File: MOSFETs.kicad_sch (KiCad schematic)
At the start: 40 parts, among them J4 Motor, J6 Sol_1, J7 Sol_2, J8 Sol_3, J9 Sol_4, Q1 IRF520N, Q2 IRF520N, Q3 IRF520N, Q4 IRF520N, Q5 IRF520N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

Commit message: working: continue at Work.
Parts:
- J4, J6, J7, J8, J9: footprint TerminalBlock_Phoenix:TerminalBlock_Phoenix_PT-1,5-2-5.0-H_1x02_P5.00mm_Horizontal -> TerminalBlock_RND:TerminalBlock_RND_205-00276_1x02_P5.00mm_Vertical
- R10, R11, R12, R13, R14, R15, R16, R17, R22, R23, R24, R25, R26, R8, R9: footprint Resistor_THT:R_Axial_DIN0309_L9.0mm_D3.2mm_P12.70mm_Horizontal -> Resistor_SMD:R_1206_3216Metric_Pad1.30x1.75mm_HandSolder
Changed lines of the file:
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@@
 			)
 		)
-		(property "Footprint" "TerminalBlock_Phoenix:TerminalBlock_Phoenix_PT-1,5-2-5.0-H_1x02_P5.00mm_Horizontal"
+		(property "Footprint" "TerminalBlock_RND:TerminalBlock_RND_205-00276_1x02_P5.00mm_Vertical"
 			(at 204.47 55.88 0)
 			(effects
@@
 			)
 		)
-		(property "Footprint" "Resistor_THT:R_Axial_DIN0309_L9.0mm_D3.2mm_P12.70mm_Horizontal"
+		(property "Footprint" "Resistor_SMD:R_1206_3216Metric_Pad1.30x1.75mm_HandSolder"
 			(at 154.94 59.182 90)
 			(effects
@@
 			)
 		)
-		(property "Footprint" "TerminalBlock_Phoenix:TerminalBlock_Phoenix_PT-1,5-2-5.0-H_1x02_P5.00mm_Horizontal"
+		(property "Footprint" "TerminalBlock_RND:TerminalBlock_RND_205-00276_1x02_P5.00mm_Vertical"
 			(at 97.79 149.86 0)
 			(effects
@@
 			)
 		)
-		(property "Footprint" "Resistor_THT:R_Axial_DIN0309_L9.0mm_D3.2mm_P12.70mm_Horizontal"
+		(property "Footprint" "Resistor_SMD:R_1206_3216Metric_Pad1.30x1.75mm_HandSolder"
 			(at 189.738 72.39 90)
 			(effects
@@
 			)
 		)
-		(property "Footprint" "TerminalBlock_Phoenix:TerminalBlock_Phoenix_PT-1,5-2-5.0-H_1x02_P5.00mm_Horizontal"
+		(property "Footprint" "TerminalBlock_RND:TerminalBlock_RND_205-00276_1x02_P5.00mm_Vertical"
 			(at 96.52 30.48 0)
 			(effects
@@
 			)
 		)
-		(property "Footprint" "Resistor_THT:R_Axial_DIN0309_L9.0mm_D3.2mm_P12.70mm_Horizontal"
+		(property "Footprint" "Resistor_SMD:R_1206_3216Metric_Pad1.30x1.75mm_HandSolder"
 			(at 81.788 105.41 90)
 			(effects
@@
 			)
 		)
-		(property "Footprint" "Resistor_THT:R_Axial_DIN0309_L9.0mm_D3.2mm_P12.70mm_Horizontal"
+		(property "Footprint" "Resistor_SMD:R_1206_3216Metric_Pad1.30x1.75mm_HandSolder"
 			(at 48.26 153.162 90)
 			(effects
@@
 			)
 		)
-		(property "Footprint" "TerminalBlock_Phoenix:TerminalBlock_Phoenix_PT-1,5-2-5.0-H_1x02_P5.00mm_Horizontal"
+		(property "Footprint" "TerminalBlock_RND:TerminalBlock_RND_205-00276_1x02_P5.00mm_Vertical"
 			(at 96.52 88.9 0)
 			(effects
@@
 			)
 		)
-		(property "Footprint" "Resistor_THT:R_Axial_DIN0309_L9.0mm_D3.2mm_P12.70mm_Horizontal"
+		(property "Footprint" "Resistor_SMD:R_1206_3216Metric_Pad1.30x1.75mm_HandSolder"
 			(at 187.198 135.89 90)
 			(effects
@@
 			)
 		)
-		(property "Footprint" "Resistor_THT:R_Axial_DIN0309_L9.0mm_D3.2mm_P12.70mm_Horizontal"
+		(property "Footprint" "Resistor_SMD:R_1206_3216Metric_Pad1.30x1.75mm_HandSolder"
 			(at 46.99 33.782 90)
 			(effects
@@
 			)
 		)
-		(property "Footprint" "Resistor_THT:R_Axial_DIN0309_L9.0mm_D3.2mm_P12.70mm_Horizontal"
+		(property "Footprint" "Resistor_SMD:R_1206_3216Metric_Pad1.30x1.75mm_HandSolder"
 			(at 156.21 122.682 90)
 			(effects
@@
 			)
 		)
-		(property "Footprint" "Resistor_THT:R_Axial_DIN0309_L9.0mm_D3.2mm_P12.70mm_Horizontal"
+		(property "Footprint" "Resistor_SMD:R_1206_3216Metric_Pad1.30x1.75mm_HandSolder"
 			(at 79.248 166.37 90)
 			(effects
@@
 			)
 		)
-		(property "Footprint" "Resistor_THT:R_Axial_DIN0309_L9.0mm_D3.2mm_P12.70mm_Horizontal"
+		(property "Footprint" "Resistor_SMD:R_1206_3216Metric_Pad1.30x1.75mm_HandSolder"
 			(at 83.058 166.37 90)
 			(effects
@@
 			)
 		)
-		(property "Footprint" "TerminalBlock_Phoenix:TerminalBlock_Phoenix_PT-1,5-2-5.0-H_1x02_P5.00mm_Horizontal"
+		(property "Footprint" "TerminalBlock_RND:TerminalBlock_RND_205-00276_1x02_P5.00mm_Vertical"
 			(at 205.74 119.38 0)
 			(effects
@@
 			)
 		)
-		(property "Footprint" "Resistor_THT:R_Axial_DIN0309_L9.0mm_D3.2mm_P12.70mm_Horizontal"
+		(property "Footprint" "Resistor_SMD:R_1206_3216Metric_Pad1.30x1.75mm_HandSolder"
 			(at 191.008 135.89 90)
 			(effects
@@
 			)
 		)
-		(property "Footprint" "Resistor_THT:R_Axial_DIN0309_L9.0mm_D3.2mm_P12.70mm_Horizontal"
+		(property "Footprint" "Resistor_SMD:R_1206_3216Metric_Pad1.30x1.75mm_HandSolder"
 			(at 81.788 46.99 90)
 			(effects
@@
 			)
 		)
-		(property "Footprint" "Resistor_THT:R_Axial_DIN0309_L9.0mm_D3.2mm_P12.70mm_Horizontal"
+		(property "Footprint" "Resistor_SMD:R_1206_3216Metric_Pad1.30x1.75mm_HandSolder"
 			(at 185.928 72.39 90)
 			(effects
@@
 			)
 		)
-		(property "Footprint" "Resistor_THT:R_Axial_DIN0309_L9.0mm_D3.2mm_P12.70mm_Horizontal"
+		(property "Footprint" "Resistor_SMD:R_1206_3216Metric_Pad1.30x1.75mm_HandSolder"
 			(at 77.978 105.41 90)
 			(effects
@@
 			)
 		)
-		(property "Footprint" "Resistor_THT:R_Axial_DIN0309_L9.0mm_D3.2mm_P12.70mm_Horizontal"
+		(property "Footprint" "Resistor_SMD:R_1206_3216Metric_Pad1.30x1.75mm_HandSolder"
 			(at 46.99 92.202 90)
 			(effects
@@
 			)
 		)
-		(property "Footprint" "Resistor_THT:R_Axial_DIN0309_L9.0mm_D3.2mm_P12.70mm_Horizontal"
+		(property "Footprint" "Resistor_SMD:R_1206_3216Metric_Pad1.30x1.75mm_HandSolder"
 			(at 77.978 46.99 90)
 			(effects

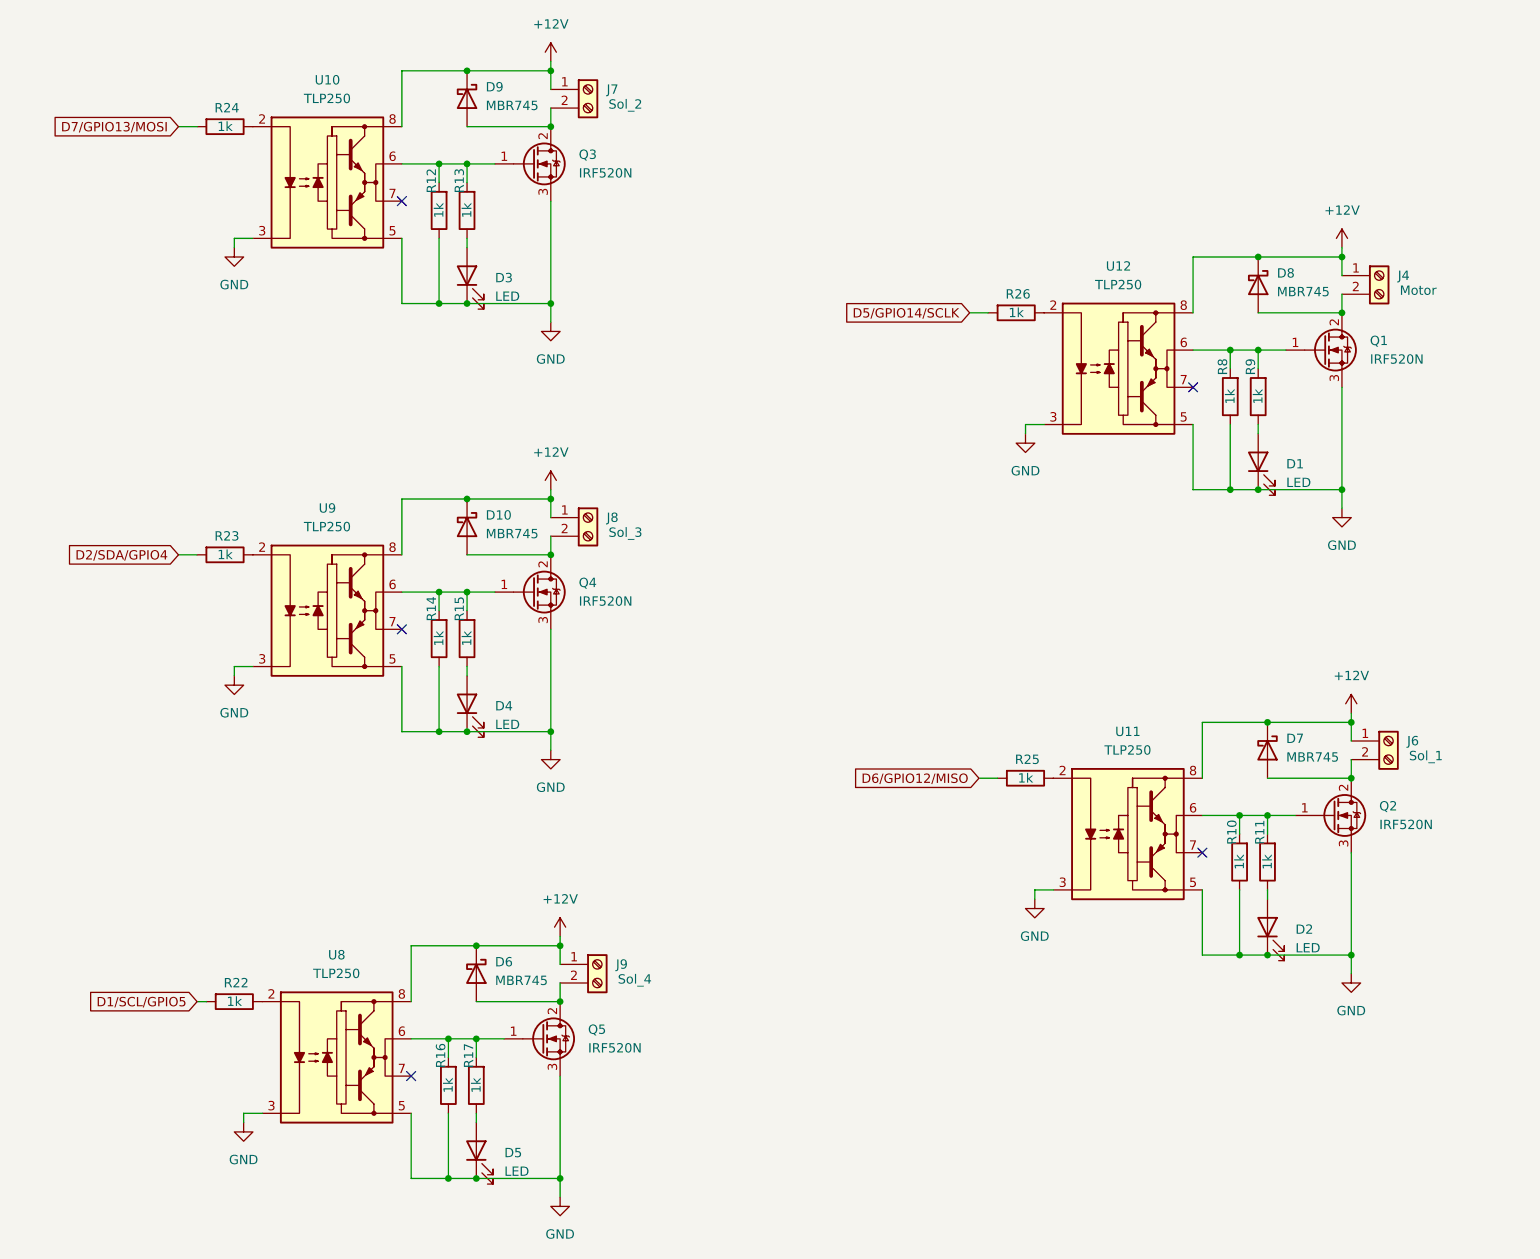
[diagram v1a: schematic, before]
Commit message: Feat: adding Buck converter + making BOM files HTML with LINKs of stores + small edits + adding polarity protection.
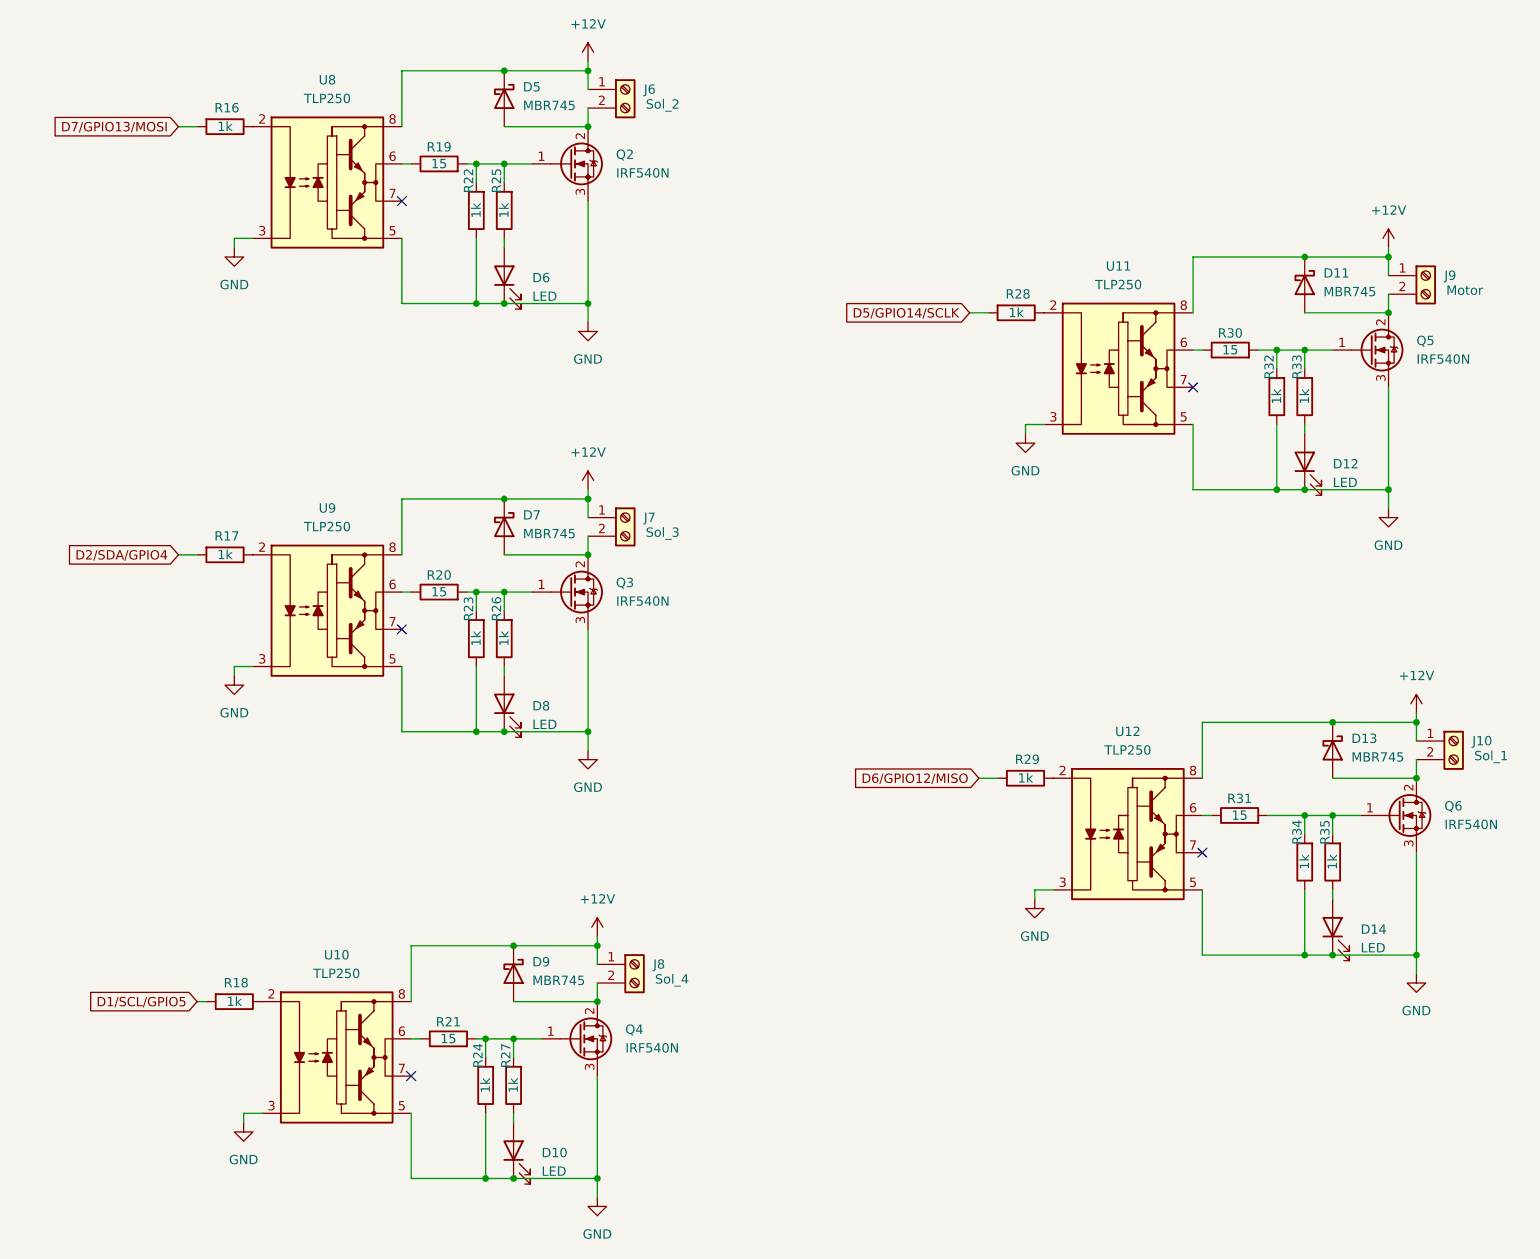
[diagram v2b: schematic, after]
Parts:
- added R19, R20, R21, R30, R31: 15, Resistor_SMD:R_1206_3216Metric_Pad1.30x1.75mm_HandSolder, symbol Device:R
- D10: renamed from D5; LINK (none) -> https://makerselectronics.com/product/smd-led-red-1206
- D11: renamed from D8; LINK (none) -> https://makerselectronics.com/product/mbr745-schottky-barri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
- D12: renamed from D1; LINK (none) -> https://makerselectronics.com/product/smd-led-red-1206
- D13: renamed from D7; LINK (none) -> https://makerselectronics.com/product/mbr745-schottky-barri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
- D14: renamed from D2; LINK (none) -> https://makerselectronics.com/product/smd-led-red-1206
- D5: renamed from D9; LINK (none) -> https://makerselectronics.com/product/mbr745-schottky-barri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
- D6: renamed from D3; LINK (none) -> https://makerselectronics.com/product/smd-led-red-1206
- D7: renamed from D10; LINK (none) -> https://makerselectronics.com/product/mbr745-schottky-barri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
- D8: renamed from D4; LINK (none) -> https://makerselectronics.com/product/smd-led-red-1206
- D9: renamed from D6; LINK (none) -> https://makerselectronics.com/product/mbr745-schottky-barri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
- J10: renamed from J6; LINK (none) -> https://makerselectronics.com/product/terminal-block-kf2edg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
- J6: renamed from J7; LINK (none) -> https://makerselectronics.com/product/terminal-block-kf2edg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
- J7: renamed from J8; LINK (none) -> https://makerselectronics.com/product/terminal-block-kf2edg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
- J8: renamed from J9; LINK (none) -> https://makerselectronics.com/product/terminal-block-kf2edg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
- J9: renamed from J4; LINK (none) -> https://makerselectronics.com/product/terminal-block-kf2edg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
- Q2: renamed from Q3; value IRF520N -> IRF540N; LINK (none) -> https://makerselectronics.com/product/irf540-n-channel-powe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
- Q3: renamed from Q4; value IRF520N -> IRF540N; LINK (none) -> https://makerselectronics.com/product/irf540-n-channel-powe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
- Q4: renamed from Q5; value IRF520N -> IRF540N; LINK (none) -> https://makerselectronics.com/product/irf540-n-channel-powe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
- Q5: renamed from Q1; value IRF520N -> IRF540N; LINK (none) -> https://makerselectronics.com/product/irf540-n-channel-powe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
- Q6: renamed from Q2; value IRF520N -> IRF540N; LINK (none) -> https://makerselectronics.com/product/irf540-n-channel-powe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
- R16: renamed from R24; LINK (none) -> https://makerselectronics.com/product/chip-resistor-smd-1kω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
- R17: renamed from R23; LINK (none) -> https://makerselectronics.com/product/chip-resistor-smd-1kω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
- R18: renamed from R22; LINK (none) -> https://makerselectronics.com/product/chip-resistor-smd-1kω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
- R22: renamed from R12; LINK (none) -> https://makerselectronics.com/product/chip-resistor-smd-1kω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
- R23: renamed from R14; LINK (none) -> https://makerselectronics.com/product/chip-resistor-smd-1kω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
- R24: renamed from R16; LINK (none) -> https://makerselectronics.com/product/chip-resistor-smd-1kω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
- R25: renamed from R13; LINK (none) -> https://makerselectronics.com/product/chip-resistor-smd-1kω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
- R26: renamed from R15; LINK (none) -> https://makerselectronics.com/product/chip-resistor-smd-1kω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
- R27: renamed from R17; LINK (none) -> https://makerselectronics.com/product/chip-resistor-smd-1kω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
- R28: renamed from R26; LINK (none) -> https://makerselectronics.com/product/chip-resistor-smd-1kω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
- R29: renamed from R25; LINK (none) -> https://makerselectronics.com/product/chip-resistor-smd-1kω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
- R32: renamed from R8; LINK (none) -> https://makerselectronics.com/product/chip-resistor-smd-1kω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
- R33: renamed from R9; LINK (none) -> https://makerselectronics.com/product/chip-resistor-smd-1kω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
- R34: renamed from R10; LINK (none) -> https://makerselectronics.com/product/chip-resistor-smd-1kω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
- R35: renamed from R11; LINK (none) -> https://makerselectronics.com/product/chip-resistor-smd-1kω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
- U10: renamed from U8; LINK (none) -> https://makerselectronics.com/product/tlp250-mosfet-driver-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
- U11: renamed from U12; LINK (none) -> https://makerselectronics.com/product/tlp250-mosfet-driver-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
- U12: renamed from U11; LINK (none) -> https://makerselectronics.com/product/tlp250-mosfet-driver-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
- U8: renamed from U10; LINK (none) -> https://makerselectronics.com/product/tlp250-mosfet-driver-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
- U9: LINK (none) -> https://makerselectronics.com/product/tlp250-mosfet-driver-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
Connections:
- net at Q2.1 (G), R22.2, R25.2: now also R19.2; no longer U8.6 (VO)
- net at Q3.1 (G), R23.2, R26.2: now also R20.2; no longer U9.6 (VO)
- net at Q5.1 (G), R32.2, R33.2: now also R30.2; no longer U11.6 (VO)
- net at Q6.1 (G), R34.2, R35.2: now also R31.2; no longer U12.6 (VO)
- net at Q4.1 (G), R24.2, R27.2: now also R21.2; no longer U10.6 (VO)
- new net: R30.1, U11.6 (VO)
- new net: R31.1, U12.6 (VO)
- new net: R20.1, U9.6 (VO)
- new net: R19.1, U8.6 (VO)
- new net: R21.1, U10.6 (VO)
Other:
- moved on the sheet: D10, D11, D12, D13, D14, D5, D6, D7, D8, D9, J10, J6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

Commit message: Feat: the board now has a circuit that manage       the switch between Battery and Adaptor Power.
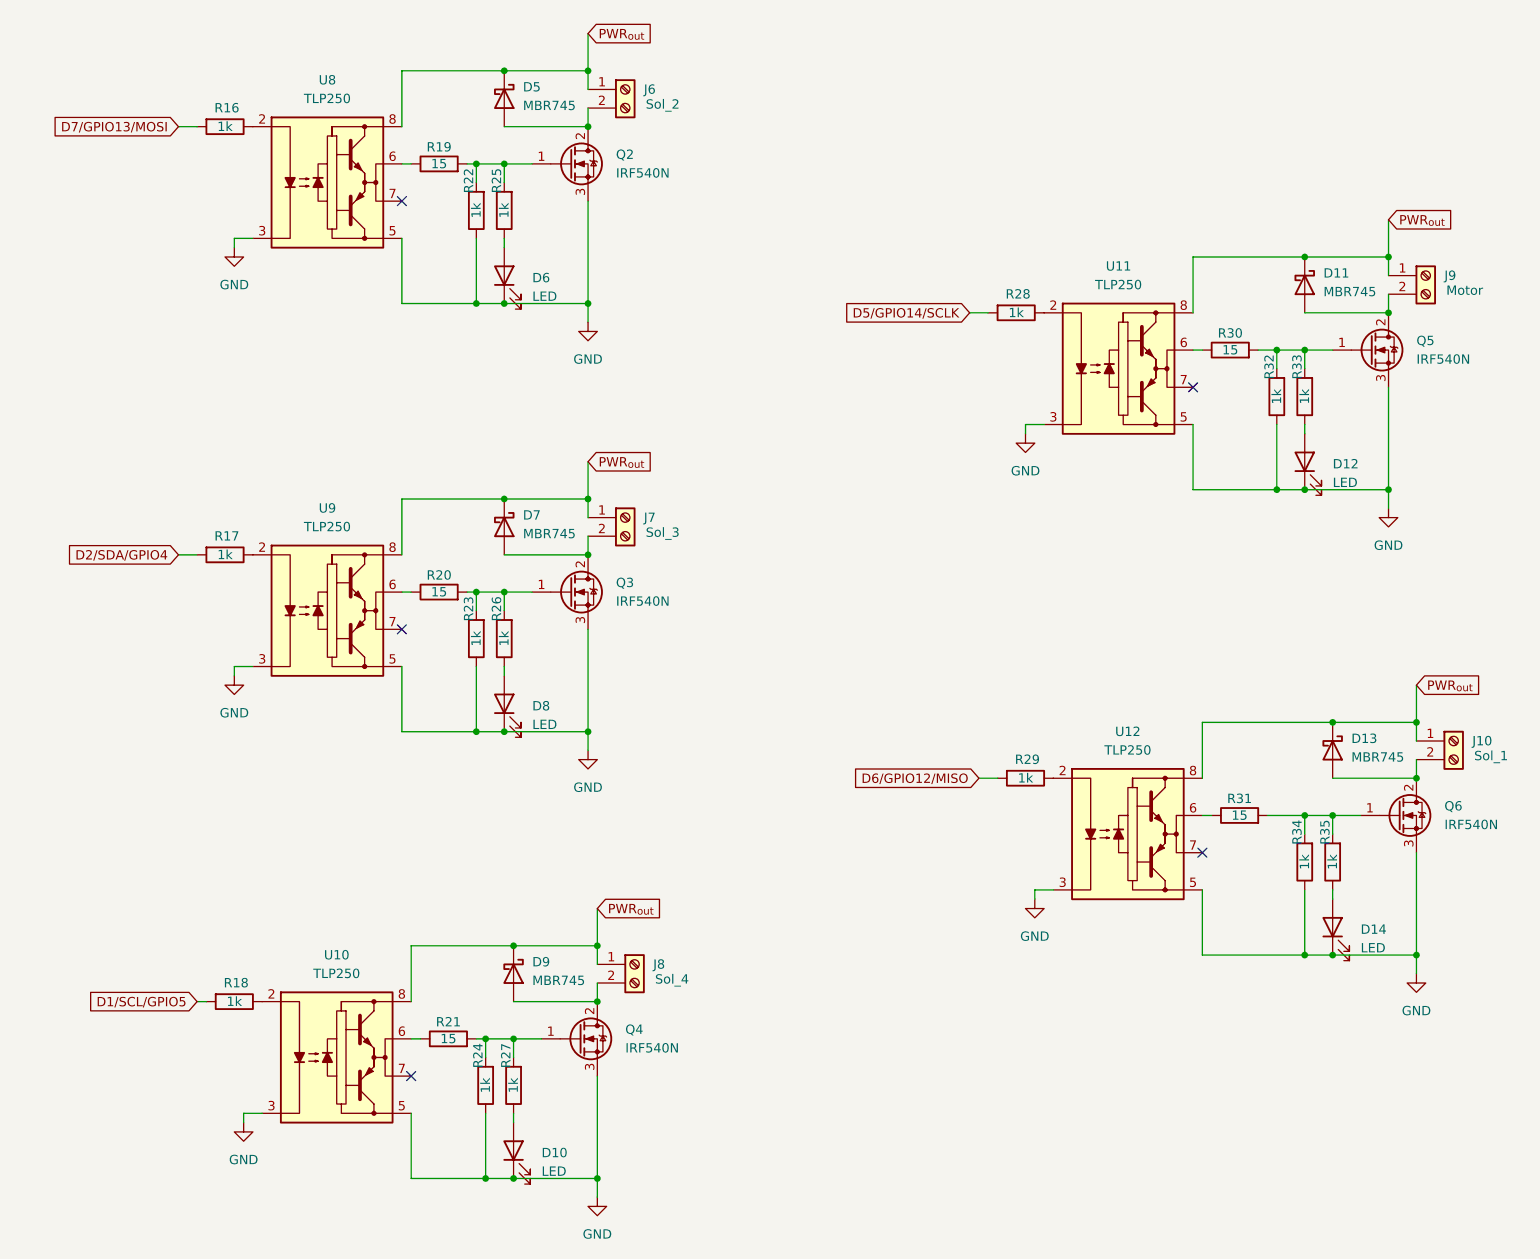
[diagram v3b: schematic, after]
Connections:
- net +12V renamed PWR_{out}
